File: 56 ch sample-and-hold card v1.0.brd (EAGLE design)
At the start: 170.8 x 36.2 mm, 141 parts, among them IC1 74HCT4051D, IC10 TL074JT, IC11 74HCT4051D, IC12 TL074JT, IC13 TL074JT, IC14 74HCT4051D, IC15 TL074JT, IC16 TL074JT, IC17 74HCT4051D, IC18 TL074JT, IC19 TL074JT, IC2 DAC8586D, IC20 74HCT4051D, IC21 TL074JT, IC22 TL074JT, IC26 74HCT4051D, IC27 TL074JT, IC28 TL074JT, IC3 TL074JT, IC5 78L05F, IC6 TL074JT, IC7 74HCT4051D, IC8 TL074JT, IC9 TL074JT, X2 FEMALE, X3 FEMALE, X4 DNM, X5 DNM, X7 FEMALE, X8 FEMALE, X9 DNM

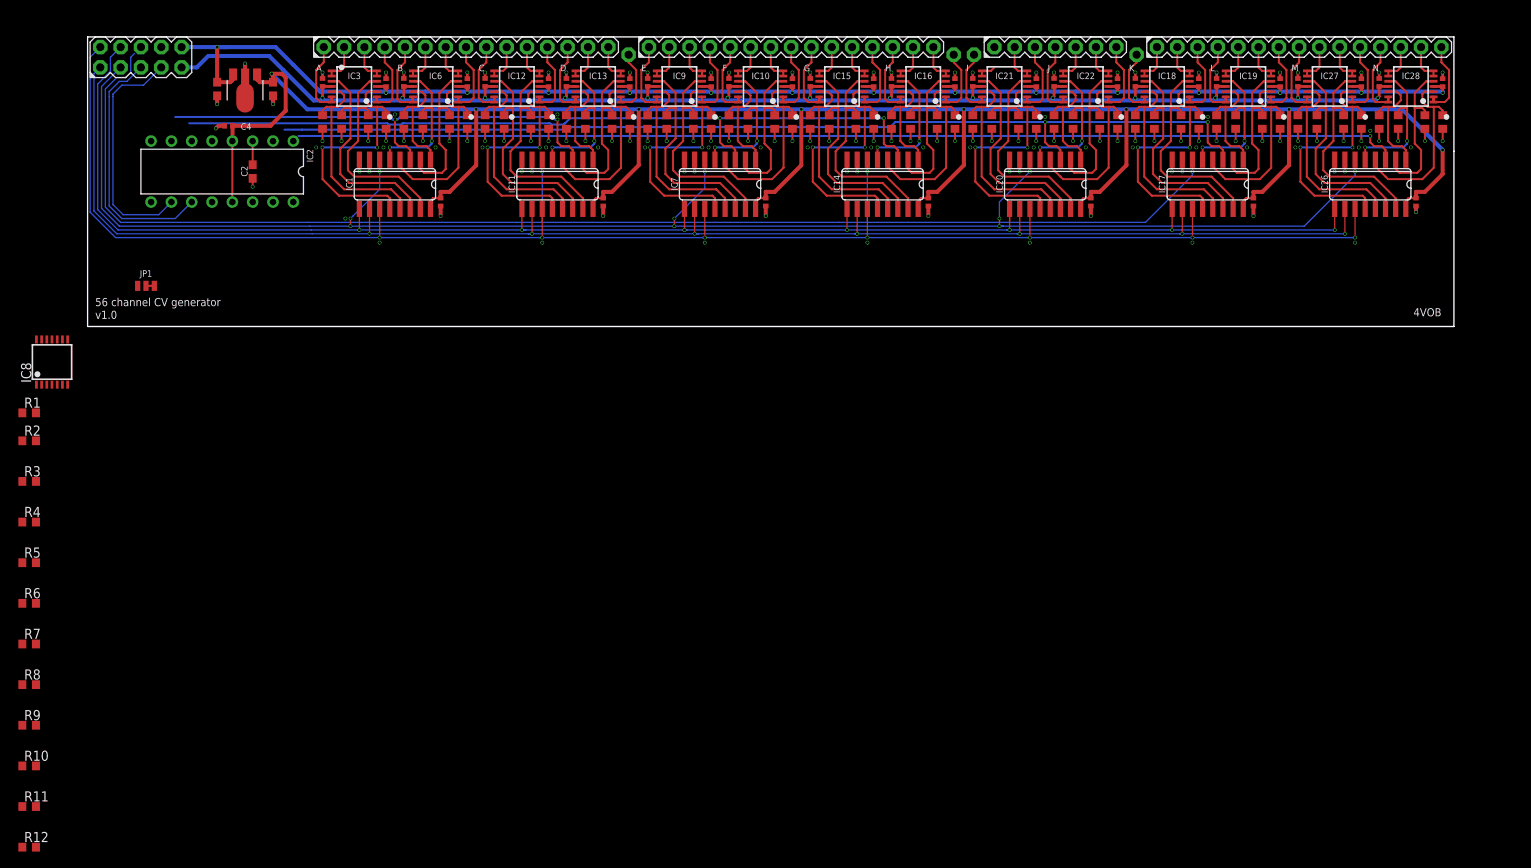
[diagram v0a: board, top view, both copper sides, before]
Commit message: Fixed ground bug, finished tracing
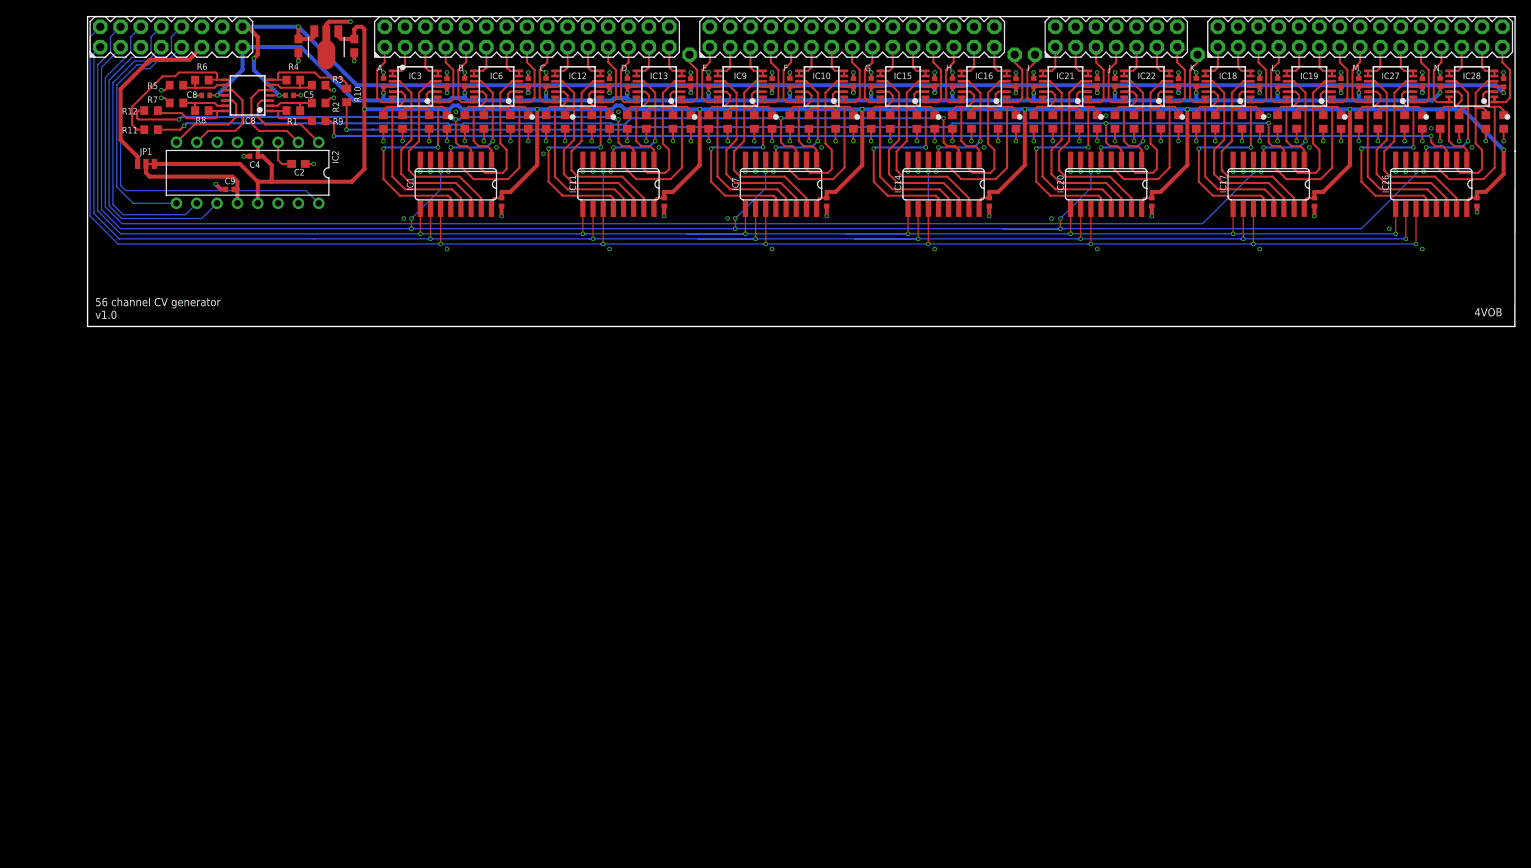
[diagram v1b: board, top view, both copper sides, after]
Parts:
- removed X1: (no value), joakim:MA05-2J
- removed X2, X3, X7: FEMALE, joakim:MA15-1J
- removed X8: FEMALE, joakim:MA07-1J
- added C5, C8, C9: 1uF, joakim:C0402-J
- added U$2, U$3, U$4: MA15-2J, joakim:MA15-2J
- added X10: (no value), joakim:MA07-2J
- added X6: (no value), joakim:MA08-2J
- moved R12 93.3 mm to (7.94, 27.0), turned to 180 degrees
- moved R10 92.7 mm to (32.4, 28.9), turned to 270 degrees
- moved R11 86.0 mm to (7.94, 24.6)
- moved R9 83.8 mm to (28.9, 25.7)
- moved R8 74.9 mm to (14.3, 27.0)
- moved R7 70.1 mm to (11.1, 27.9)
- moved R6 68.9 mm to (14.3, 30.8)
- moved R4 64.4 mm to (25.7, 30.8), turned to 180 degrees
- moved R5 62.5 mm to (11.1, 30.2)
- moved R3 61.3 mm to (28.9, 30.2), turned to 180 degrees
- moved R2 55.6 mm to (28.9, 27.9), turned to 180 degrees
- moved R1 50.2 mm to (25.7, 27.0), turned to 180 degrees
- moved IC8 41.3 mm to (20.0, 28.9), turned to 90 degrees
- moved JP1 15.2 mm to (7.30, 20.3)
- moved C1 11.5 mm to (33.3, 35.1)
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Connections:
- removed net GND: X1.8
- removed net INH_2: IC11.6, IC14.6, IC17.6, X1.6
- removed net N$6: R1.1, R2.2
- removed net V+: IC8.4
- removed net V-: IC8.11
- new net INH_0: IC1.6, IC20.6, IC26.6, IC7.6, X6.3
- new net LDAC: IC2.16, X6.9
- net !SYNC: now also X6.10
- net +12V: now also C5.1, IC8.4, X6.16; no longer X1.10
- net +3V3: now also X6.11
- net -12V: now also C8.2, IC8.11, X6.15; no longer X1.9
- net A0: now also X6.2; no longer X1.2
- net A1: now also X6.1; no longer X1.1
- net A2: now also X6.4; no longer X1.4
- net AGND: now also C5.2, C8.1, C9.2, X6.14; no longer IC2.16
- net INH_1: now also IC11.6, IC14.6, IC17.6, X6.6; no longer IC1.6, IC20.6, IC26.6, IC7.6, X1.3
- net N$1: now also C9.1
- net N$2: now also R1.1, R2.2
- net OUT_0: now also U$2.1; no longer X2.1
- net OUT_1: now also U$2.3; no longer X2.2
- net OUT_10: now also U$2.21; no longer X2.11
- net OUT_11: now also U$2.23; no longer X2.12
- net OUT_12: now also U$2.25; no longer X2.13
- net OUT_13: now also U$2.27; no longer X2.14
- net OUT_14: now also U$2.29; no longer X2.15
- net OUT_16: now also U$3.1; no longer X3.1
- net OUT_17: now also U$3.3; no longer X3.2
- net OUT_18: now also U$3.5; no longer X3.3
- net OUT_19: now also U$3.7; no longer X3.4
- net OUT_2: now also U$2.5; no longer X2.3
- net OUT_20: now also U$3.9; no longer X3.5
- net OUT_21: now also U$3.11; no longer X3.6
- net OUT_22: now also U$3.13; no longer X3.7
- net OUT_23: now also U$3.15; no longer X3.8
- net OUT_24: now also U$3.17; no longer X3.9
- net OUT_25: now also U$3.19; no longer X3.10
- net OUT_26: now also U$3.21; no longer X3.11
- net OUT_27: now also U$3.23; no longer X3.12
- net OUT_28: now also U$3.25; no longer X3.13
- net OUT_29: now also U$3.27; no longer X3.14
- net OUT_3: now also U$2.7; no longer X2.4
- net OUT_30: now also U$3.29; no longer X3.15
- net OUT_33: now also X10.1; no longer X8.1
- net OUT_34: now also X10.3; no longer X8.2
- net OUT_35: now also X10.5; no longer X8.3
- net OUT_36: now also X10.7; no longer X8.4
- net OUT_37: now also X10.9; no longer X8.5
- net OUT_38: now also X10.11; no longer X8.6
- net OUT_39: now also X10.13; no longer X8.7
- net OUT_4: now also U$2.9; no longer X2.5
- net OUT_41: now also U$4.1; no longer X7.1
- net OUT_42: now also U$4.3; no longer X7.2
- net OUT_43: now also U$4.5; no longer X7.3
- net OUT_44: now also U$4.7; no longer X7.4
- net OUT_45: now also U$4.9; no longer X7.5
- net OUT_46: now also U$4.11; no longer X7.6
- net OUT_47: now also U$4.13; no longer X7.7
- net OUT_48: now also U$4.15; no longer X7.8
- net OUT_49: now also U$4.17; no longer X7.9
- net OUT_5: now also U$2.11; no longer X2.6
- net OUT_50: now also U$4.19; no longer X7.10
- net OUT_51: now also U$4.21; no longer X7.11
- net OUT_52: now also U$4.23; no longer X7.12
- net OUT_53: now also U$4.25; no longer X7.13
- net OUT_54: now also U$4.27; no longer X7.14
- net OUT_55: now also U$4.29; no longer X7.15
- net OUT_6: now also U$2.13; no longer X2.7
- net OUT_7: now also U$2.15; no longer X2.8
- net OUT_8: now also U$2.17; no longer X2.9
- net OUT_9: now also U$2.19; no longer X2.10
- net SCK: now also X6.7; no longer X1.7
- net SDA: now also X6.8; no longer X1.5
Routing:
- net INH_0: track 0.00 -> 243.2 mm, vias 0 -> 10
- net INH_2: track 178.1 -> 0.00 mm, vias 3 -> 0
- net LDAC: track 0.00 -> 47.6 mm
- net A1: track 199.5 -> 243.2 mm
- net A2: track 198.6 -> 241.8 mm
- net !SYNC: track 0.00 -> 33.3 mm
- net +5V: track 283.7 -> 311.3 mm
- net +3V3: track 0.00 -> 22.6 mm
- net +12V: track 197.5 -> 220.1 mm, vias 15 -> 17
- net INH_1: track 210.9 -> 189.0 mm, vias 10 -> 3
- net DAC_BUF_3: track 0.00 -> 19.3 mm
- net A0: track 207.0 -> 223.3 mm
- net N$1: track 0.00 -> 16.2 mm
- net DAC_4: track 60.9 -> 75.3 mm, vias 2 -> 3
- net AGND: track 142.0 -> 155.4 mm, vias 144 -> 148
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- added copper zone on layer 15, net AGND
- added copper zone on layer 2, net AGND
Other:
- board size 170.8 x 36.2 mm -> 178.4 x 38.7 mm
- board text added: "!SYN"
- board text added: "3V3"
- board text added: "IH0"
- board text added: "LDC"
- board text removed: "IH2"

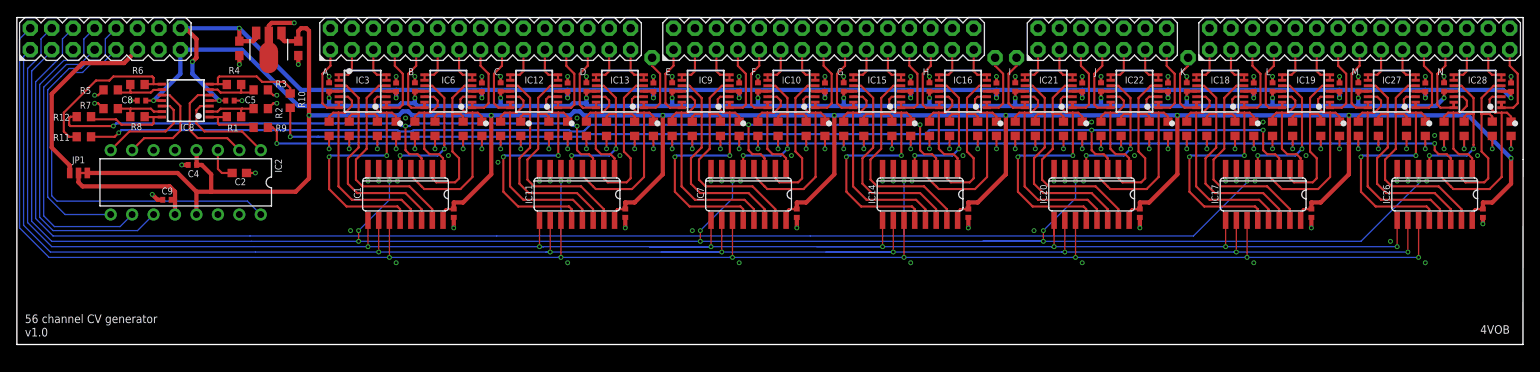
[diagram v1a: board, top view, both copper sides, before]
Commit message: Changed dac footprint
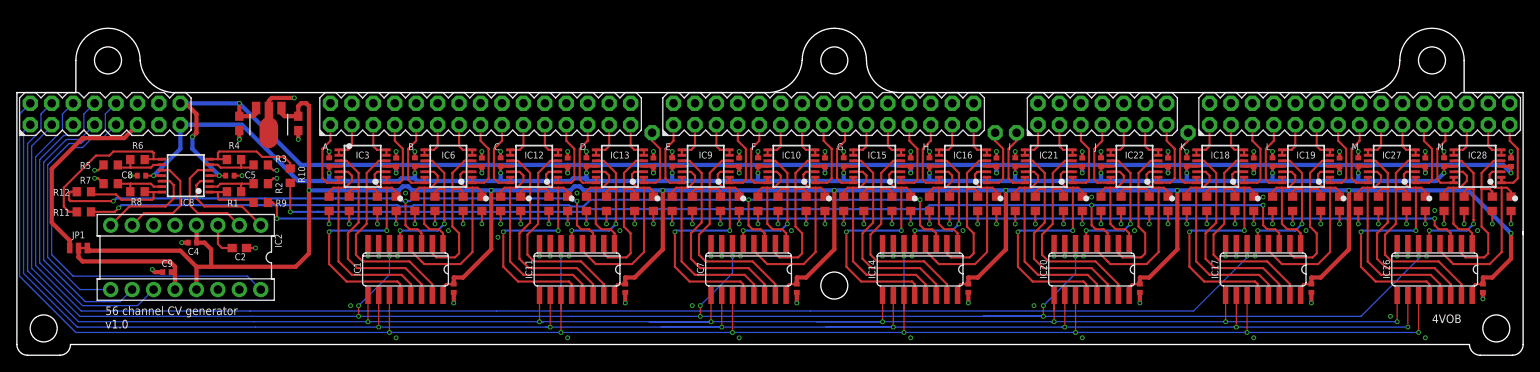
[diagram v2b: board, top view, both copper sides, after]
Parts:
- IC2: value DAC8586D -> DAC8586F; device joakim:DIL16J -> joakim:DIL16-FM-CON
- U$2, U$3, U$4: value MA15-2J -> FEMALE
- X10, X6: value (none) -> FEMALE
- moved U$1 46.9 mm to (119.4, 7.78)
- moved C4 9.21 mm to (20.8, 12.1)
- moved C1 8.89 mm to (33.3, 26.2)
- moved C108 8.89 mm to (166.8, 16.7)
- moved C109 8.89 mm to (164.6, 16.7)
- moved C11 8.89 mm to (42.7, 16.7)
- moved C110 8.89 mm to (161.3, 16.7)
- moved C111 8.89 mm to (158.9, 16.7)
- moved C112 8.89 mm to (166.8, 21.6)
- moved C113 8.89 mm to (158.9, 21.6)
- moved C114 8.89 mm to (177.0, 16.7)
- moved C115 8.89 mm to (174.8, 16.7)
- moved C116 8.89 mm to (171.4, 16.7)
- moved C117 8.89 mm to (169.1, 16.7)
- moved C118 8.89 mm to (177.0, 21.6)
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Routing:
- net SCK: track 34.7 -> 32.6 mm
- net SDA: track 41.0 -> 39.0 mm
- net INH_0: track 243.2 -> 241.3 mm
- net INH_1: track 189.0 -> 187.1 mm
- net A2: track 241.8 -> 239.9 mm
- net A0: track 223.3 -> 221.5 mm
- net A1: track 243.2 -> 241.3 mm
- net LDAC: track 47.6 -> 46.5 mm
- net !SYNC: track 33.3 -> 32.2 mm
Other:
- outline, holes or cut-outs redrawn

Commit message: v1.0 ready for production
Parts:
- C2: value 150nF -> 100nF
- IC2: value DAC8586F -> DAC8565F
- U$2, U$3, U$4: value FEMALE -> MA15-2J-FEMALE
- X10: value FEMALE -> MA07-2J-FEMALE
- X6: value FEMALE -> MA08-2J-FEMALE
